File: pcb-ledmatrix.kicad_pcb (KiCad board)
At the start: 2 copper layers, 216 x 89 mm, 301 parts, among them J1 USB_C_Receptacle_USB2.0_16P, J2 Conn_01x04_Pin, J3 Conn_01x04_Pin, J4 Conn_01x04_Pin, Q1 SS8050, SW1 SW_Push, SW2 SW_Push, U1 USBLC6-2SC6, U2 ESP32-C3-WROOM-02, U3 SPX3819M5-L-3-3, Y1 32.768kHz

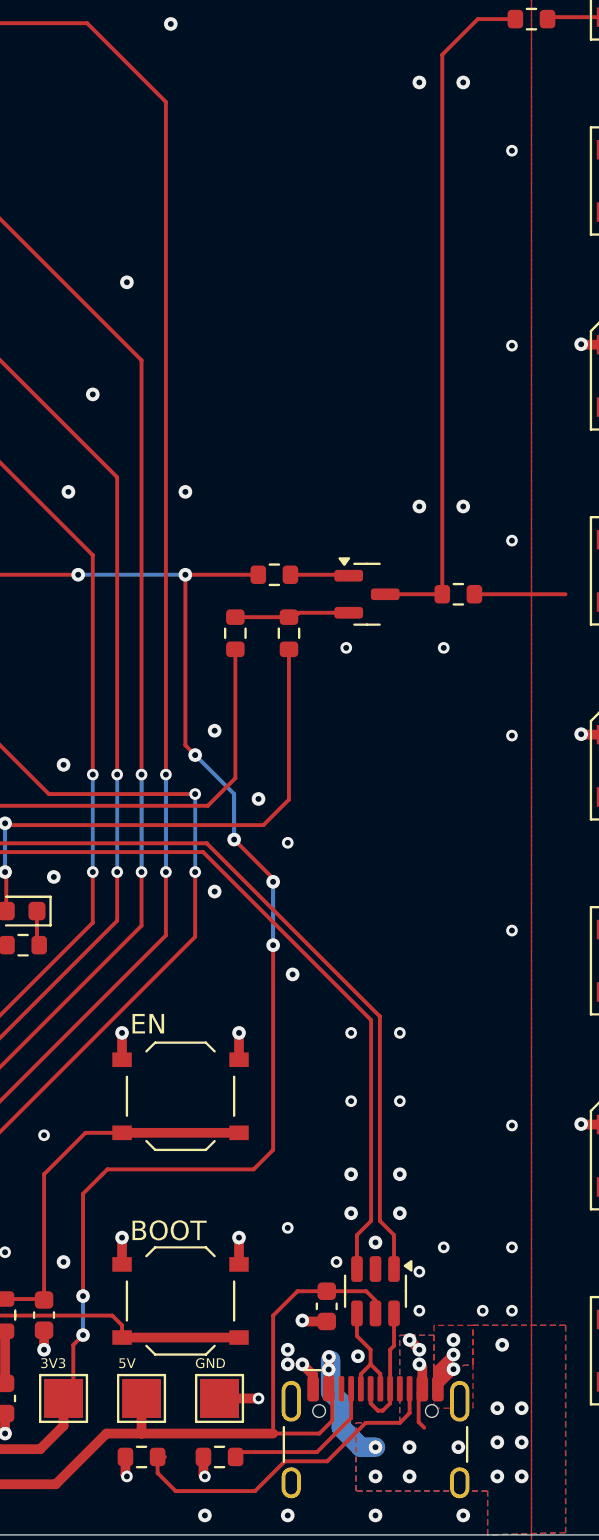
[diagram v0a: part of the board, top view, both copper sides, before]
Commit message: change level shifter in schematic
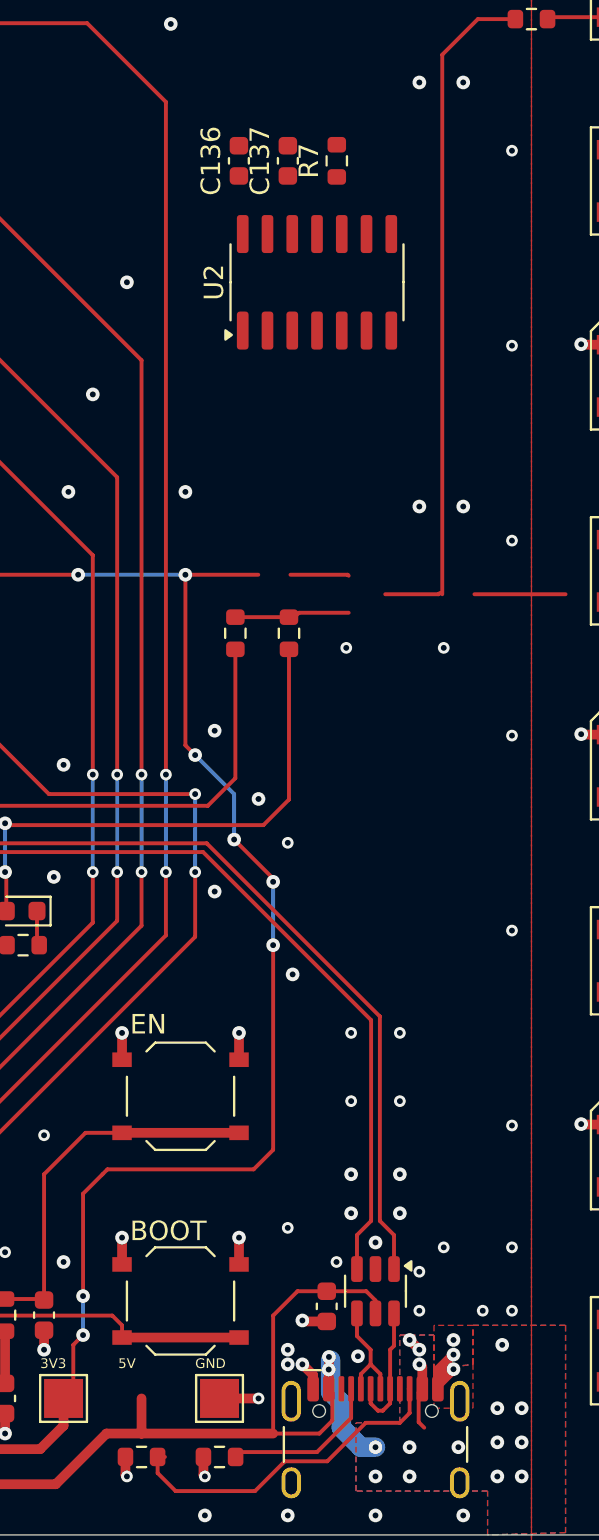
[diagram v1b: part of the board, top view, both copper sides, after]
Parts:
- removed Q1: SS8050, Package_TO_SOT_SMD:SOT-23
- removed the R12 at (89.8, 66.8)
- removed R13: 6k8, Resistor_SMD:R_0603_1608Metric
- removed TP7: 5V, TestPoint:TestPoint_Pad_2.0x2.0mm
- added C136: 100n, Capacitor_SMD:C_0603_1608Metric, F.Cu at (88.0, 45.5)
- added C137: 1u, Capacitor_SMD:C_0603_1608Metric, F.Cu at (90.5, 45.5)
- added R7: 0, Resistor_SMD:R_0603_1608Metric, F.Cu at (93.0, 45.5)
- added U2: 74AHCT125, Package_SO:SOIC-14_3.9x8.7mm_P1.27mm, F.Cu at (92.0, 51.8)
- renumbered C135 to C129, C138 to C130, C136 to C131, C137 to C132, C130 to C135, C129 to C138, C132 to C139, C131 to C140, D130 to D129, D129 to D130, J3 to J1, J4 to J2, J2 to J3, J1 to J4, R16 to R1, R14 to R10, R8 to R11, R15 to R12, R10 to R2, R17 to R3, R9 to R4, R11 to R5, R2 to R6, R1 to R8, R3 to R9, SW2 to SW1, SW1 to SW2, TP6 to TP1, TP5 to TP2, U2 to U1, U1 to U4
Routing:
- net Net-(Q1-B): track 3.01 -> 0.00 mm
- net (no net): track 0.00 -> 3.01 mm

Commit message: finisch layout, add prod files
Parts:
- added R13: 0, Resistor_SMD:R_0603_1608Metric, F.Cu at (89.5, 62.8)
- moved R7 18.0 mm to (87.8, 62.8)
- moved C136 16.4 mm to (93.5, 61.0), turned to 0 degrees
- moved U2 14.9 mm to (96.5, 66.0)
- moved C137 13.8 mm to (93.5, 59.0), turned to 0 degrees
- moved R5 2.25 mm to (90.5, 72.0)
- moved R4 2.25 mm to (87.8, 72.0)
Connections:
- U2 pad 3: Net-(R10-Pad1) -> Net-(R13-Pad1)
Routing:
- net +5V: track 70.1 -> 83.2 mm
- net MC_LED_OUT: track 5.91 -> 16.1 mm
- net Net-(R13-Pad1): track 0.00 -> 9.01 mm
- net MC_3V3: track 126.3 -> 122.6 mm
- net (no net): track 3.01 -> 0.00 mm
- net Net-(R10-Pad1): track 35.0 -> 32.1 mm
- net GND: track 388.5 -> 390.9 mm, vias 376 -> 404
- net MC_IO3: track 52.5 -> 50.2 mm
- net MC_IO10: track 59.8 -> 57.6 mm
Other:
- board text added: "LED Matrix Rev 1 06/2025"
